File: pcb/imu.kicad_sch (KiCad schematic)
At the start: 4 parts

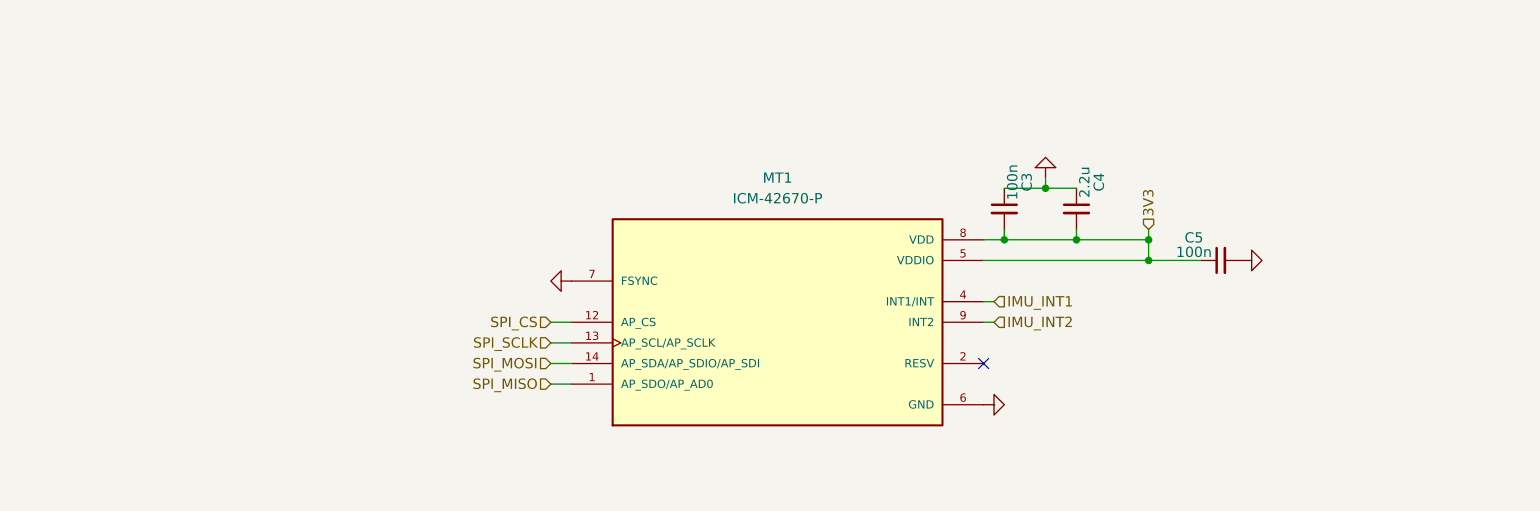
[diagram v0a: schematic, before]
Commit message: driver and buck converter layout
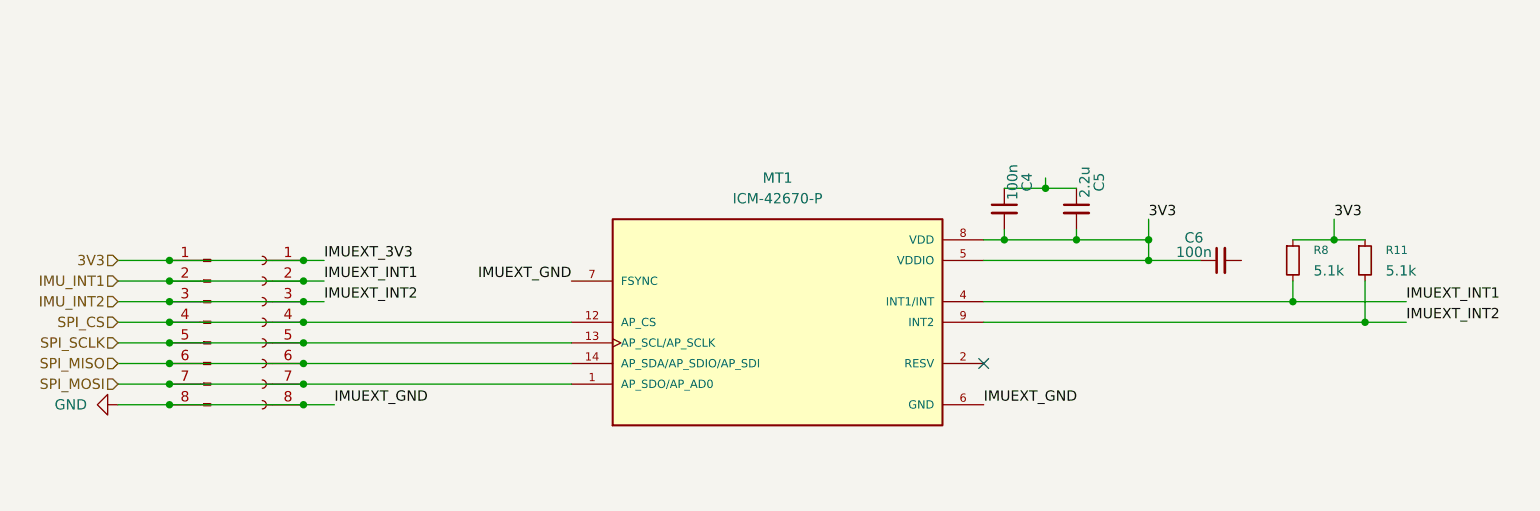
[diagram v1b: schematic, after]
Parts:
- added J7: Conn_01x08_Pin, Connector_PinSocket_2.54mm:PinSocket_2x04_P2.54mm_Vertical, symbol Connector:Conn_01x08_Pin
- added J8: Conn_01x08_Socket, Connector_PinSocket_2.54mm:PinSocket_2x04_P2.54mm_Vertical, symbol Connector:Conn_01x08_Socket
- added R11, R8: 5.1k, Resistor_SMD:R_0603_1608Metric, symbol Device:R_Small
- C4: renamed from C3; footprint (none) -> Capacitor_SMD:C_0603_1608Metric
- C5: renamed from C4; footprint (none) -> Capacitor_SMD:C_0805_2012Metric
- C6: renamed from C5; footprint (none) -> Capacitor_SMD:C_0603_1608Metric
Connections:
- net 3V3: now also J7.1 (Pin_1), J8.1 (Pin_1), R11.1, R8.1
- net GND: now also J7.8 (Pin_8), J8.8 (Pin_8); no longer C4.1, C5.1, C6.2
- net IMU_INT1: now also J7.2 (Pin_2), J8.2 (Pin_2), R8.2
- net IMU_INT2: now also J7.3 (Pin_3), J8.3 (Pin_3), R11.2
- net SPI_CS: now also J7.4 (Pin_4), J8.4 (Pin_4)
- net SPI_MISO: now also MT1.14 (AP_SDA/AP_SDIO/AP_SDI), J7.6 (Pin_6), J8.6 (Pin_6); no longer MT1.1 (AP_SDO/AP_AD0)
- net SPI_MOSI: now also MT1.1 (AP_SDO/AP_AD0), J7.7 (Pin_7), J8.7 (Pin_7); no longer MT1.14 (AP_SDA/AP_SDIO/AP_SDI)
- net SPI_SCLK: now also J7.5 (Pin_5), J8.5 (Pin_5)
- new net: C4.1, C5.1

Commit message: routing
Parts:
- removed J8: Conn_01x08_Socket, Connector_PinSocket_2.54mm:PinSocket_2x04_P2.54mm_Vertical, symbol Connector:Conn_01x08_Socket
- removed R11, R8: 5.1k, Resistor_SMD:R_0603_1608Metric, symbol Device:R_Small
- added TP12, TP13, TP14, TP15, TP17, TP18, TP19, TP20: TestPoint, Equilibot:TestPoint_Pad_1.0x1.0mm, symbol Connector:TestPoint
- MT1: footprint ICM-42670-P:XDCR_ICM-42670-P -> Equilibot:XDCR_ICM-42670-P
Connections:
- net 3V3: now also J7.7 (Pin_7), TP19.1; no longer J7.1 (Pin_1)
- net GND: now also C4.1, C5.1, C6.2, TP20.1
- net IMU_INT1: now also J7.6 (Pin_6), TP18.1; no longer J7.2 (Pin_2)
- net IMU_INT2: now also J7.5 (Pin_5), TP17.1; no longer J7.3 (Pin_3)
- net SPI_CS: now also J7.1 (Pin_1), TP12.1; no longer J7.4 (Pin_4)
- net SPI_MISO: now also J7.4 (Pin_4), MT1.1 (AP_SDO/AP_AD0), TP15.1; no longer J7.6 (Pin_6), MT1.14 (AP_SDA/AP_SDIO/AP_SDI)
- net SPI_MOSI: now also J7.3 (Pin_3), MT1.14 (AP_SDA/AP_SDIO/AP_SDI), TP14.1; no longer J7.7 (Pin_7), MT1.1 (AP_SDO/AP_AD0)
- net SPI_SCLK: now also J7.2 (Pin_2), TP13.1; no longer J7.5 (Pin_5)

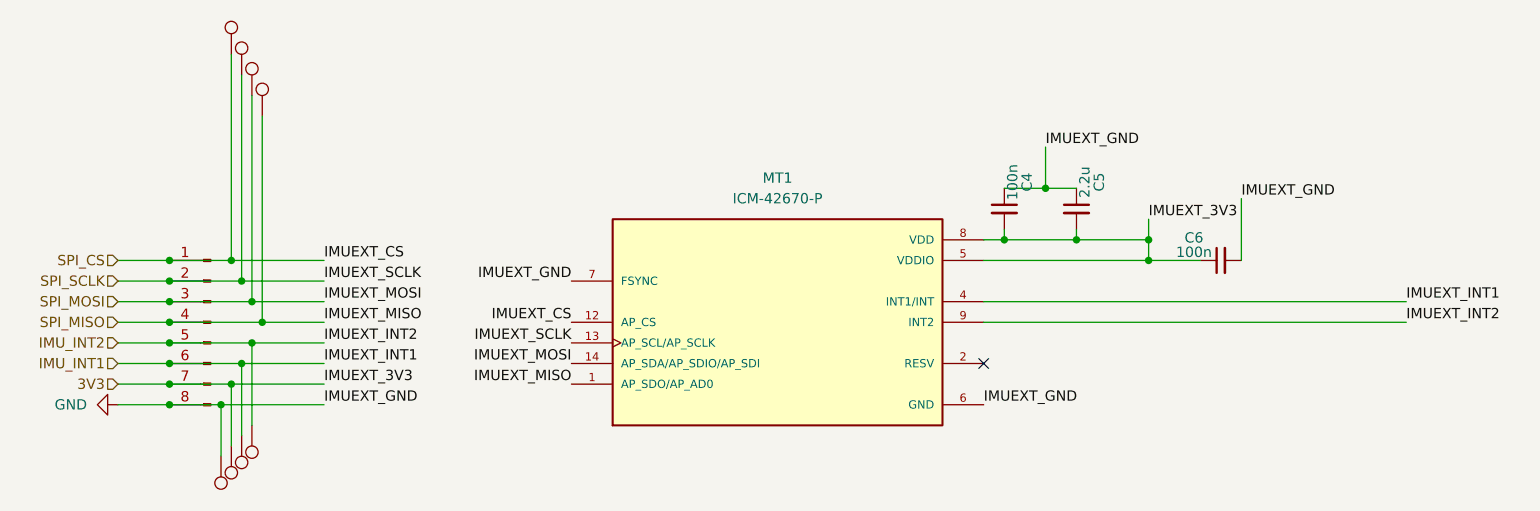
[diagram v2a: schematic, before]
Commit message: add jlcpcb part numbers
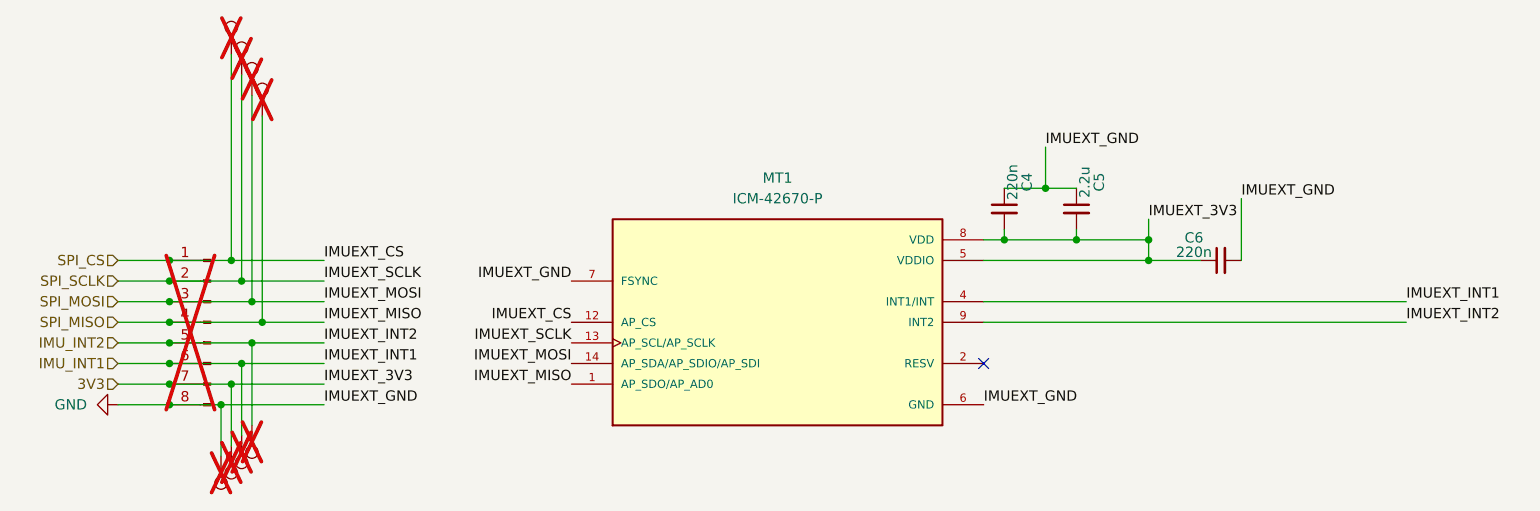
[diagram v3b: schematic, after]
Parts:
- C4, C6: value 100n -> 220n; JLCPCB Part (none) -> C21120
- C5: JLCPCB Part (none) -> C377773
- J7, TP12, TP13, TP14, TP15, TP17, TP18, TP19, TP20: now not fitted
- MT1: JLCPCB Part (none) -> C3288646

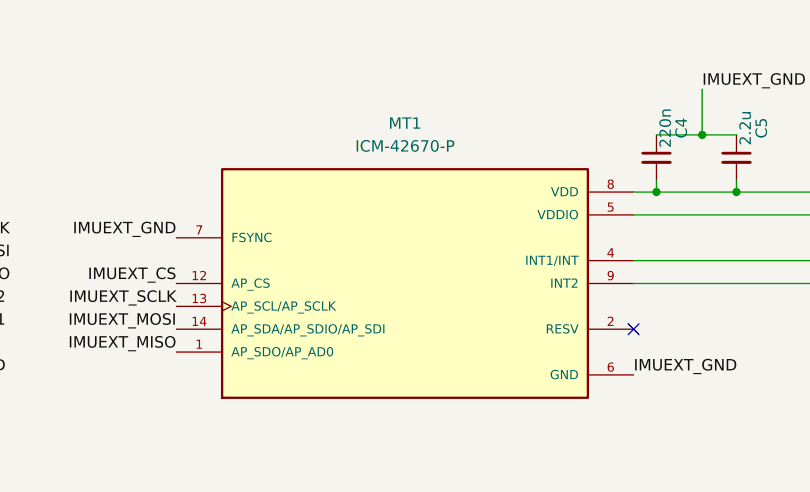
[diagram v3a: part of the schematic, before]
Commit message: change layout of extern led board to not show vias
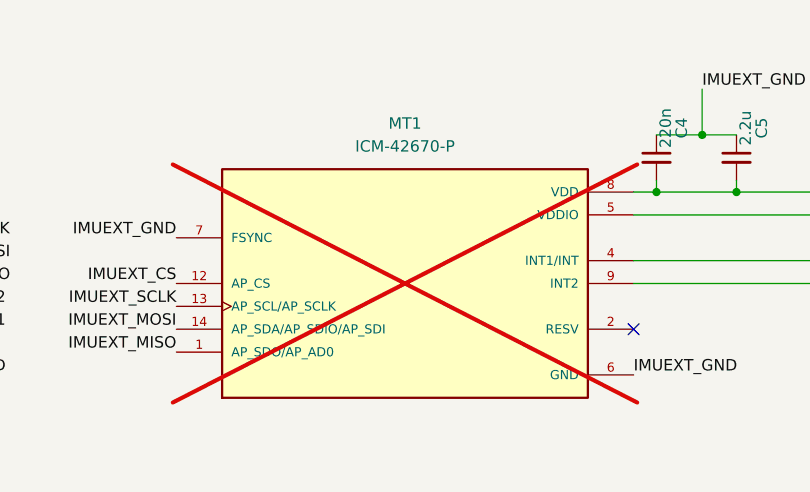
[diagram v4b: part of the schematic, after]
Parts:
- MT1: now not fitted
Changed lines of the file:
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@@
 		(in_bom yes)
 		(on_board yes)
-		(dnp no)
+		(dnp yes)
 		(fields_autoplaced yes)
 		(property "Reference" "MT1"
